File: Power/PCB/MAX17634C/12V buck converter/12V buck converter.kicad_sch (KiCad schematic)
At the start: 11 parts, among them IC1 MAX17634

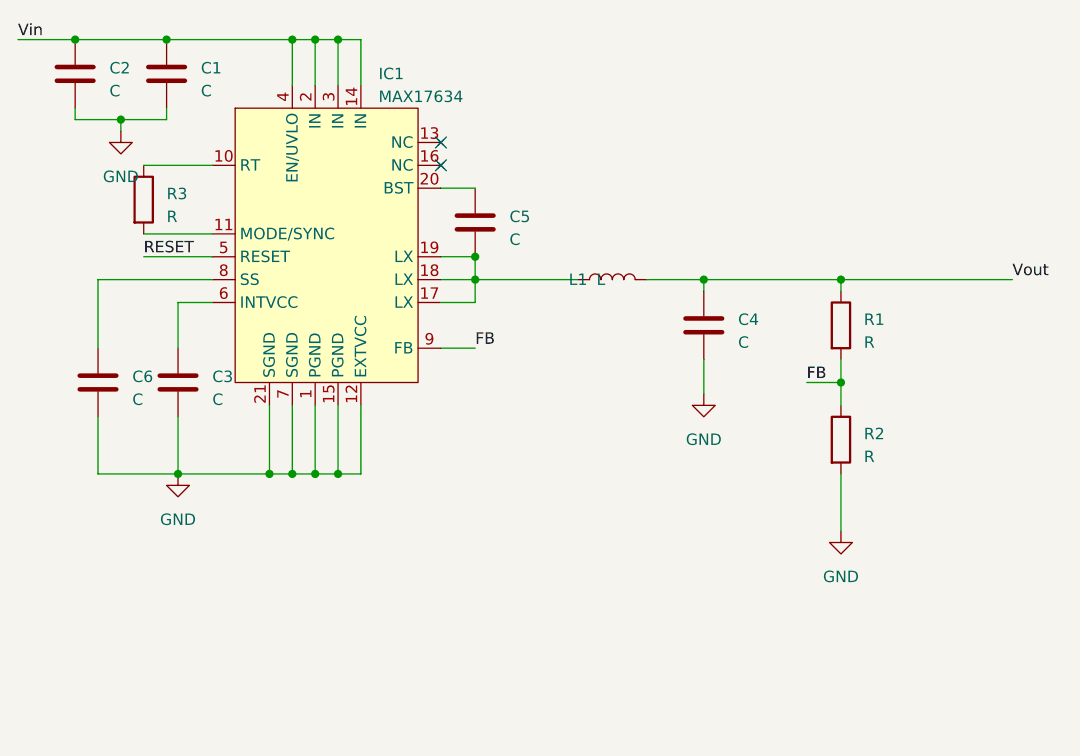
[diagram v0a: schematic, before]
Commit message: Revert "Update pcb"
This reverts commit eaa0f94790ef4127411d201ada7ecce6da68ceff.
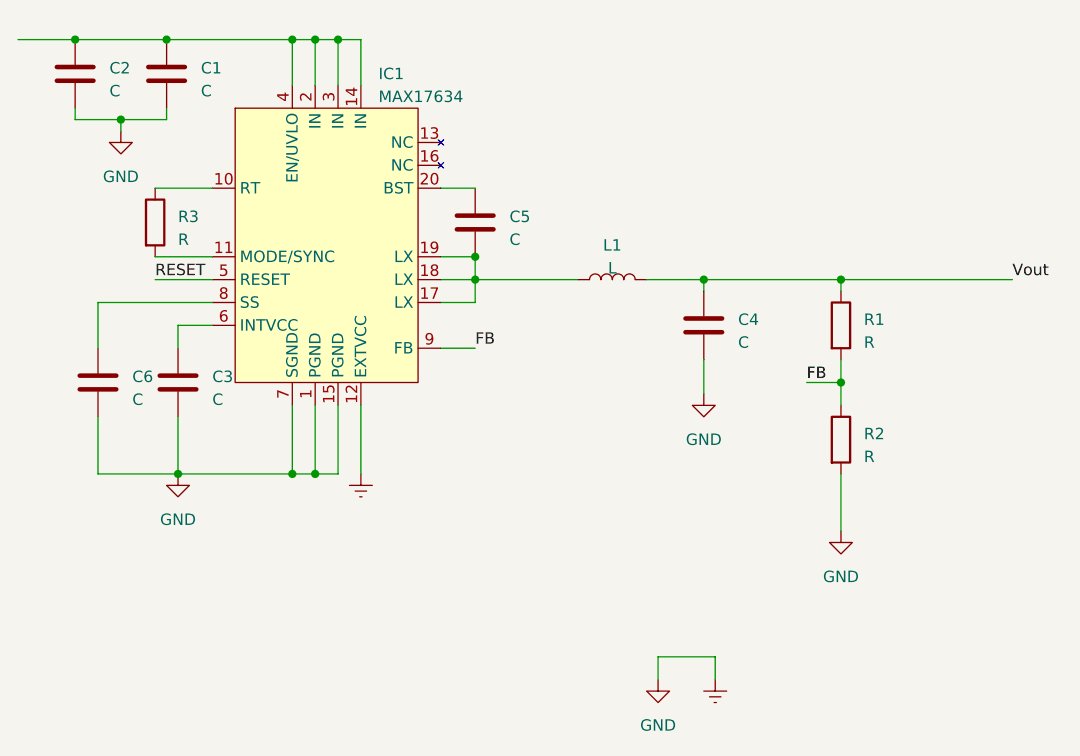
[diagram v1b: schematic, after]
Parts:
- IC1: Order https://nl.farnell.com/analog-devices/max17634catp/dc-dc-co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 -> (none)
- L1: footprint Inductor_SMD:L_6.3x6.3_H3 -> (none)
- R1, R2, R3: footprint Resistor_SMD:R_0402_1005Metric -> (none)
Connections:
- net GND renamed Earth
- net Earth: no longer IC1.21 (SGND)
- net Vin: no longer names the net of C1.1, C2.1, IC1.14 (IN), IC1.2 (IN), IC1.3 (IN), IC1.4 (EN/UVLO)
- no-connect marks 2 -> 0
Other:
- moved on the sheet: R3

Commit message: Pcb test
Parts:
- removed IC1: MAX17634, Package_DFN_QFN:TQFN-20-1EP_4x4mm_P0.5mm_EP2.9x2.9mm, symbol Audio_DSP:MAX17634
- added IC1: MAX17634C, Package_DFN_QFN:TQFN-20-1EP_4x4mm_P0.5mm_EP2.9x2.9mm, symbol Audio_DSP:MAX17634C
- added R4: R, Resistor_SMD:R_0402_1005Metric, symbol Device:R
- C1, C2, C3, C5, C6: footprint (none) -> Capacitor_SMD:C_0402_1005Metric
- C4: footprint (none) -> Capacitor_SMD:C_Elec_4x5.8
- L1: footprint (none) -> Inductor_SMD:L_6.3x6.3_H3
- R1, R2, R3: footprint (none) -> Resistor_SMD:R_0402_1005Metric
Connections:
- net FB: now also IC1.9 (FB)
- net RESET: now also IC1.5 (RESET)
- net Vin: now reaches C1.1, C2.1
- net Vin: now also IC1.14 (IN), IC1.2 (IN), IC1.3 (IN), IC1.4 (EN/UVLO)
- net at R3.1: now also IC1.10 (RT)
- net at R3.2: now also IC1.11 (MODE/SYNC)
- net at C6.1: now also IC1.8 (SS)
- net at C5.2, L1.1: now also IC1.17 (LX), IC1.18 (LX), IC1.19 (LX)
- net at C5.1: now also IC1.20 (BST)
- net at C3.1: now also IC1.6 (INTVCC)
- net Earth renamed GND
- net GND: now also IC1.1 (PGND), IC1.12 (EXTVCC), IC1.15 (PGND), IC1.7 (SGND)
